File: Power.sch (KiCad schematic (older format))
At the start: 77 parts, among them Q10 AOD514, Q11 AOD514, Q14 FK3303010L, Q15 FK3303010L, Q16 FK3303010L, Q17 FK3303010L, Q18 FK3303010L, Q19 FK3303010L, Q3 FK3303010L, Q4 FK3303010L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

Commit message: Fix voltage regulator trim resistors
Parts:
- removed R57, R58: 22k6, IPC7351-Nominal:RESC1608X50, symbol R-0603
- added R114, R115, R58: 22k6, IPC7351-Nominal:RESC1005X40, symbol R-0402
- added R57: 100k, IPC7351-Nominal:RESC1005X40, symbol R-0402
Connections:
- net GND: now also R115.2, R57.2, R58.2
- net at VREG1.2 (TRIM): now also R114.1
- net at VREG2.2 (TRIM): now also R58.1
- new net: R114.2, R115.1, R57.1

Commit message: Remove unneeded discharge FETs
PCF8575 can sink the current directly
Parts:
- removed Q19, Q3, Q7, Q8: FK3303010L, manuf:PANASONIC-SSSMini3-F2-B, symbol FK3303010L
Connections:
- net DISCH_1V2 is gone; now on net ~DISCH_1V2: U2.20 (P17)
- net DISCH_1V5 is gone; now on net ~DISCH_1V5: U2.11 (P07)
- net DISCH_3VA is gone; now on net ~DISCH_3VA: U2.13 (P10)
- net DISCH_3VB is gone; now on net ~DISCH_3VB: U2.14 (P11)
- net ~DISCH_3VA: now reaches R65.2
- net ~DISCH_3VB: now reaches R66.2
- net ~DISCH_1V5: now reaches R67.2
- net ~DISCH_1V2: now reaches R62.2

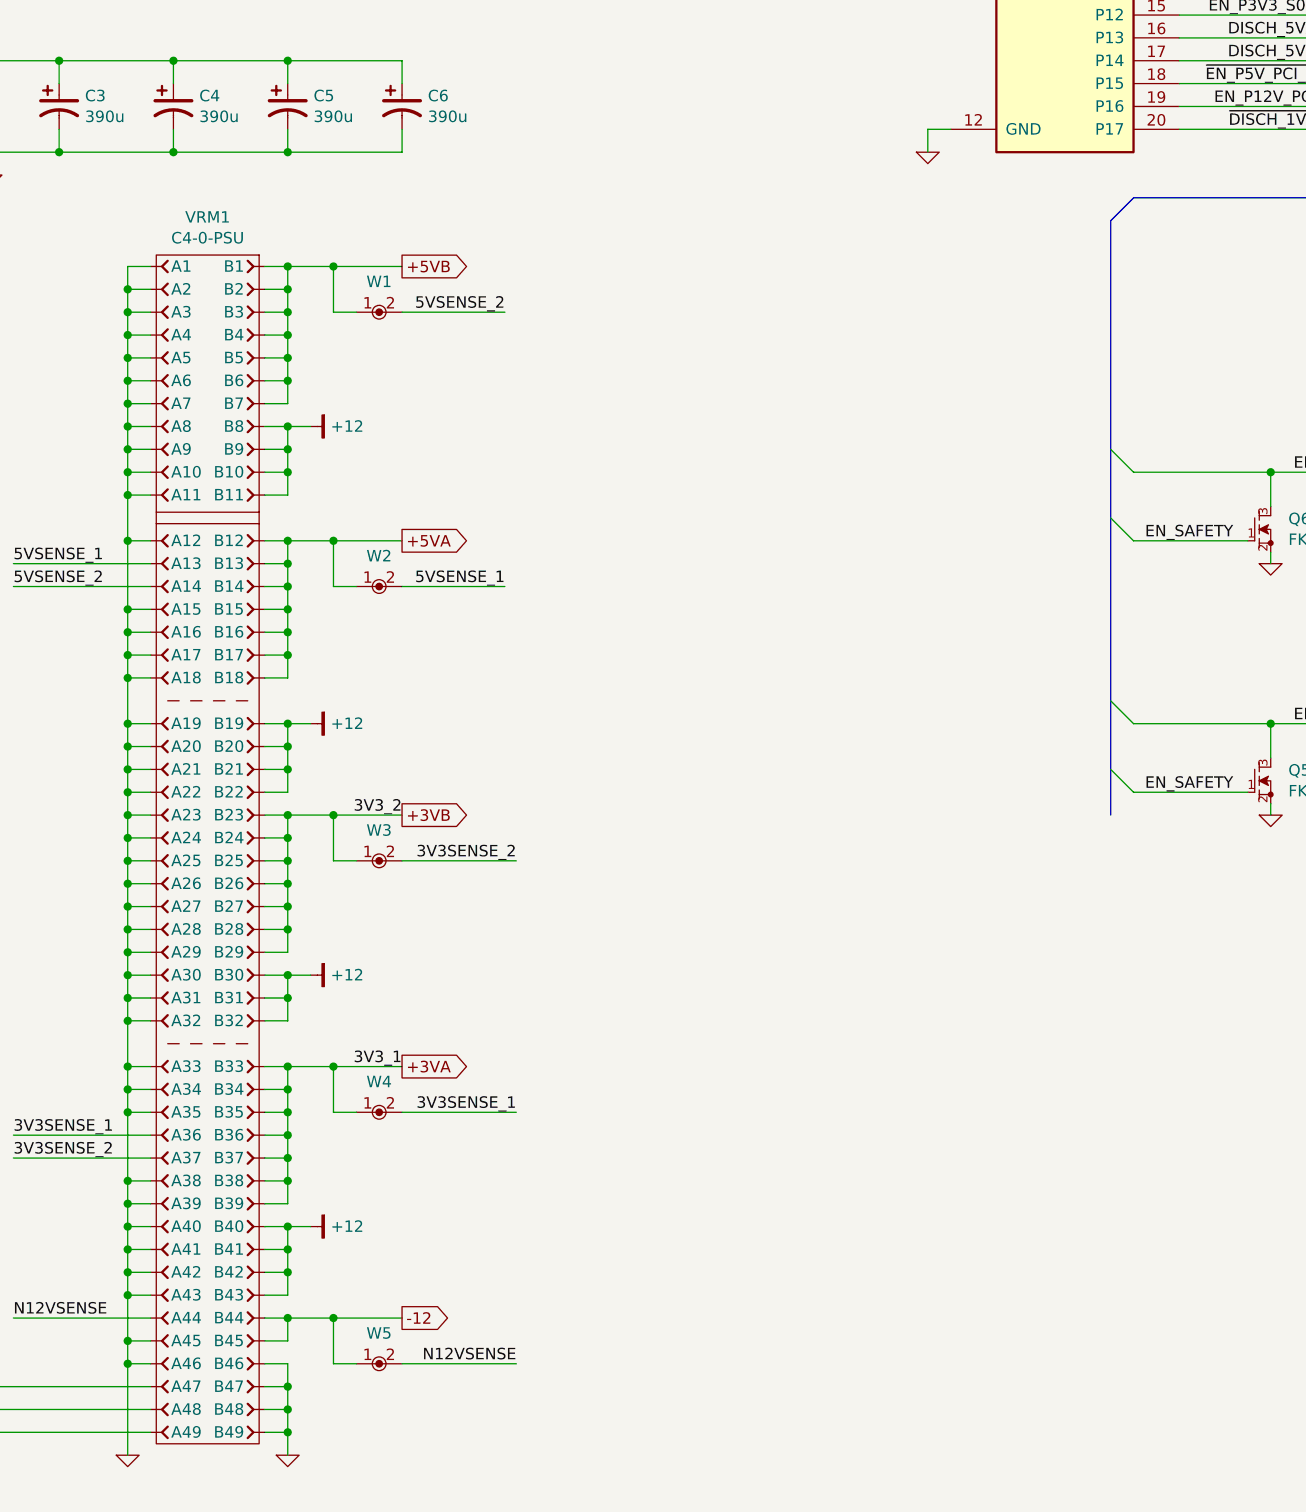
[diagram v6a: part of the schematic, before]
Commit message: Gather and assign all I2C addresses
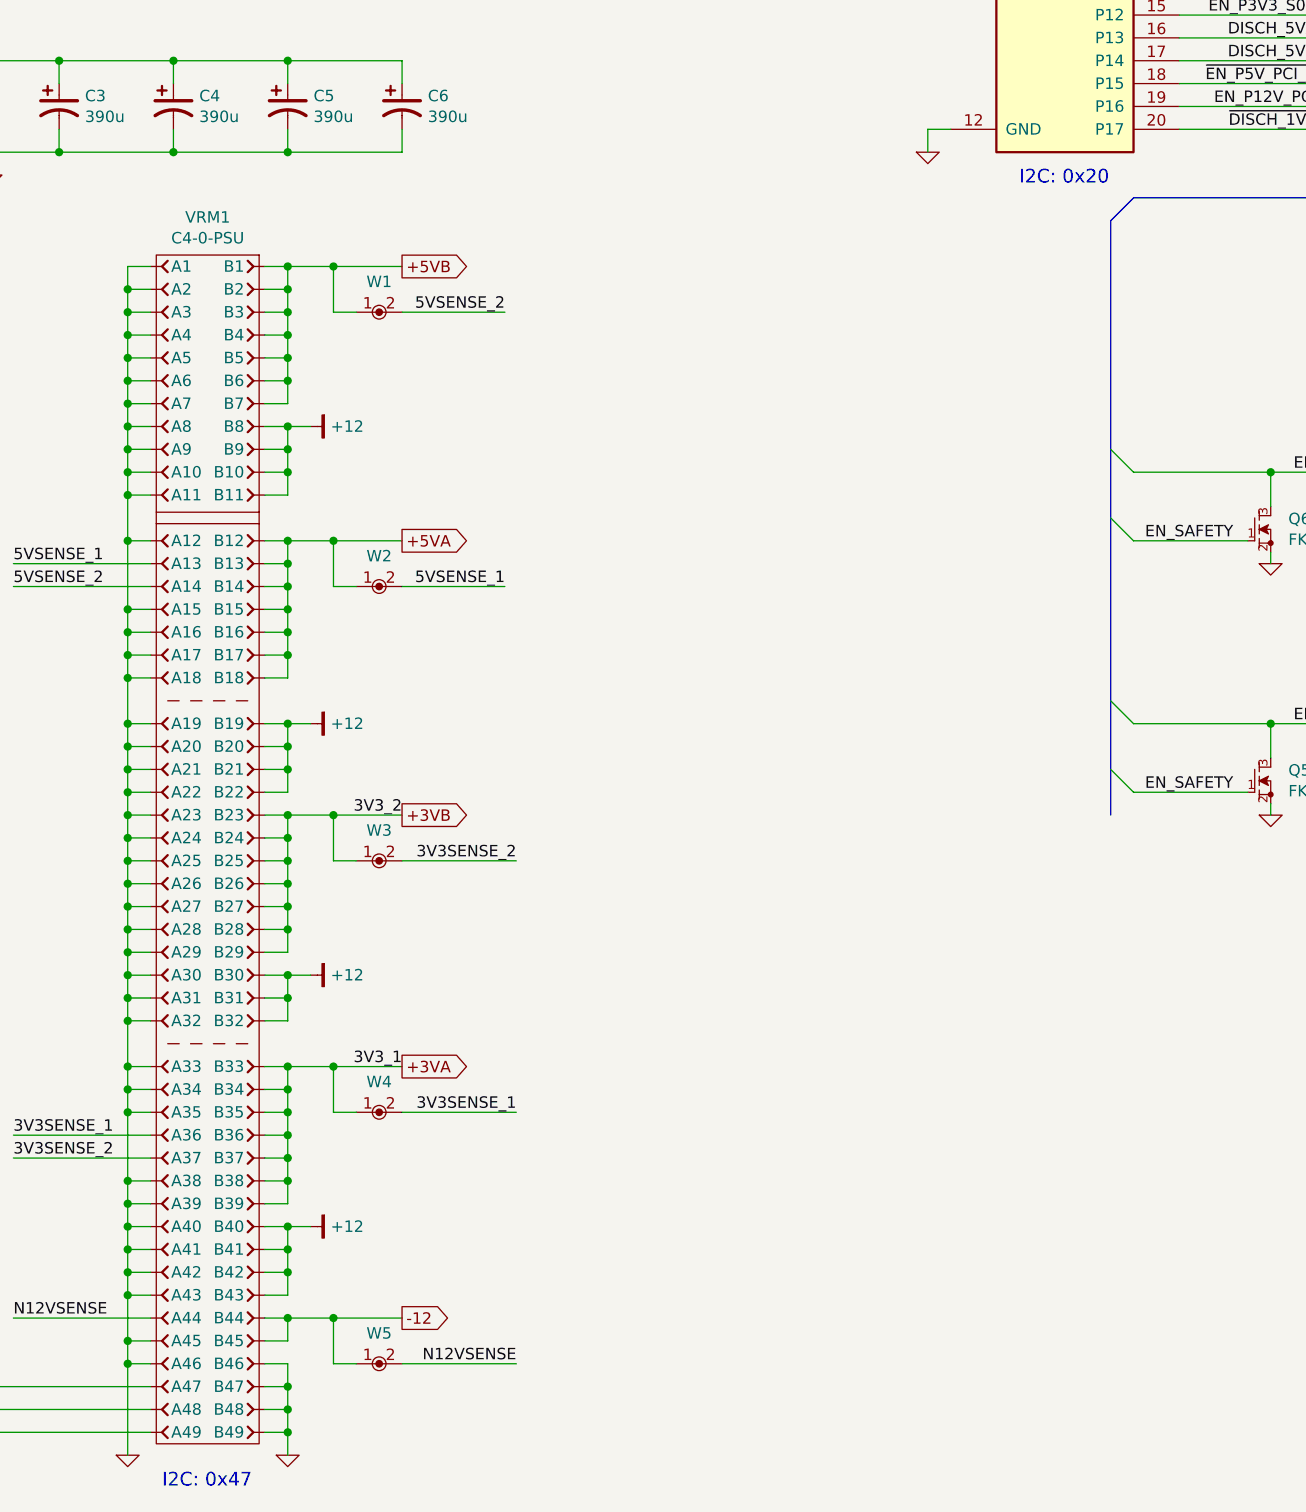
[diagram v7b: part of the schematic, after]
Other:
- note added: "I2C: 0x20"
- note added: "I2C: 0x47"
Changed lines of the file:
@@
 	1    0    0    -1
 $EndComp
+Text Notes 2650 10150 0    60   ~ 0
+I2C: 0x47
+Text Notes 6400 4450 0    60   ~ 0
+I2C: 0x20
 $EndSCHEMATC
